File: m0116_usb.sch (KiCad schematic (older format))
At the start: 182 parts, among them J1 AVR-ISP-6, J2 Conn_01x04, J3 Conn_01x04, U1 ATmega32A-PU

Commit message: change ucontroller to ATmega32u4
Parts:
- removed Boot1: Boot, Button_Switch_THT:SW_PUSH_6mm, symbol Switch:SW_Push
- removed C1: 4.7u, Capacitor_THT:CP_Radial_D5.0mm_P2.50mm, symbol Device:CP1
- removed C2, C3: 0.1u, Capacitor_THT:C_Disc_D3.0mm_W2.0mm_P2.50mm, symbol Device:C
- removed U1: ATmega32A-PU, Package_DIP:DIP-40_W15.24mm_Socket, symbol MCU_Microchip_ATmega:ATmega32A-PU
- removed XTAL1: Crystal, Crystal:Crystal_HC49-4H_Vertical, symbol Device:Crystal
- added C?: 1u, symbol Device:C_Small
- added C? (x4): 0.1u, Capacitor_THT:C_Disc_D6.0mm_W2.5mm_P5.00mm, symbol Device:C_Small
- added C?: 10u, Capacitor_THT:C_Disc_D6.0mm_W2.5mm_P5.00mm, symbol Device:C_Small
- added R?: 10k, Resistor_THT:R_Axial_DIN0207_L6.3mm_D2.5mm_P10.16mm_Horizontal, symbol Device:R
- added U?: ATmega32U4-AU, Package_QFP:TQFP-44_10x10mm_P0.8mm, symbol MCU_Microchip_ATmega:ATmega32U4-AU
- added X?: Crystal, symbol Device:Crystal_GND24_Small
- D10, D11, D12, D13, D14, D15, D16, D17, D18, D19, D20, D21, D22, D23, D24, D25, D26, D27, D28, D29, D3, D30, D31, D32, D33, D34, D35, D36, D37, D38, D39, D4, D40, D41, D42, D43, D44, D45, D46, D47, D48, D49, D5, D50, D51, D52, D53, D54, D55, D56, D57, D58, D59, D6, D60, D61, D62, D63, D64, D65, D66, D67, D68, D69, D7, D70, D71, D72, D73, D74, D75, D76, D77, D78, D79, D8, D80, D81, D82, D83, D9: footprint Diode_THT:D_DO-35_SOD27_P7.62mm_Horizontal -> Diode_SMD:D_SOD-123
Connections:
- net labels added: XTAL1, XTAL2
- net labels removed: boot
- wire segments 280 -> 308
- no-connect marks 0 -> 4
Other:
- moved on the sheet: C4, C5, D1, D10, D11, D12, D13, D14, D15, D16, D17, D18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

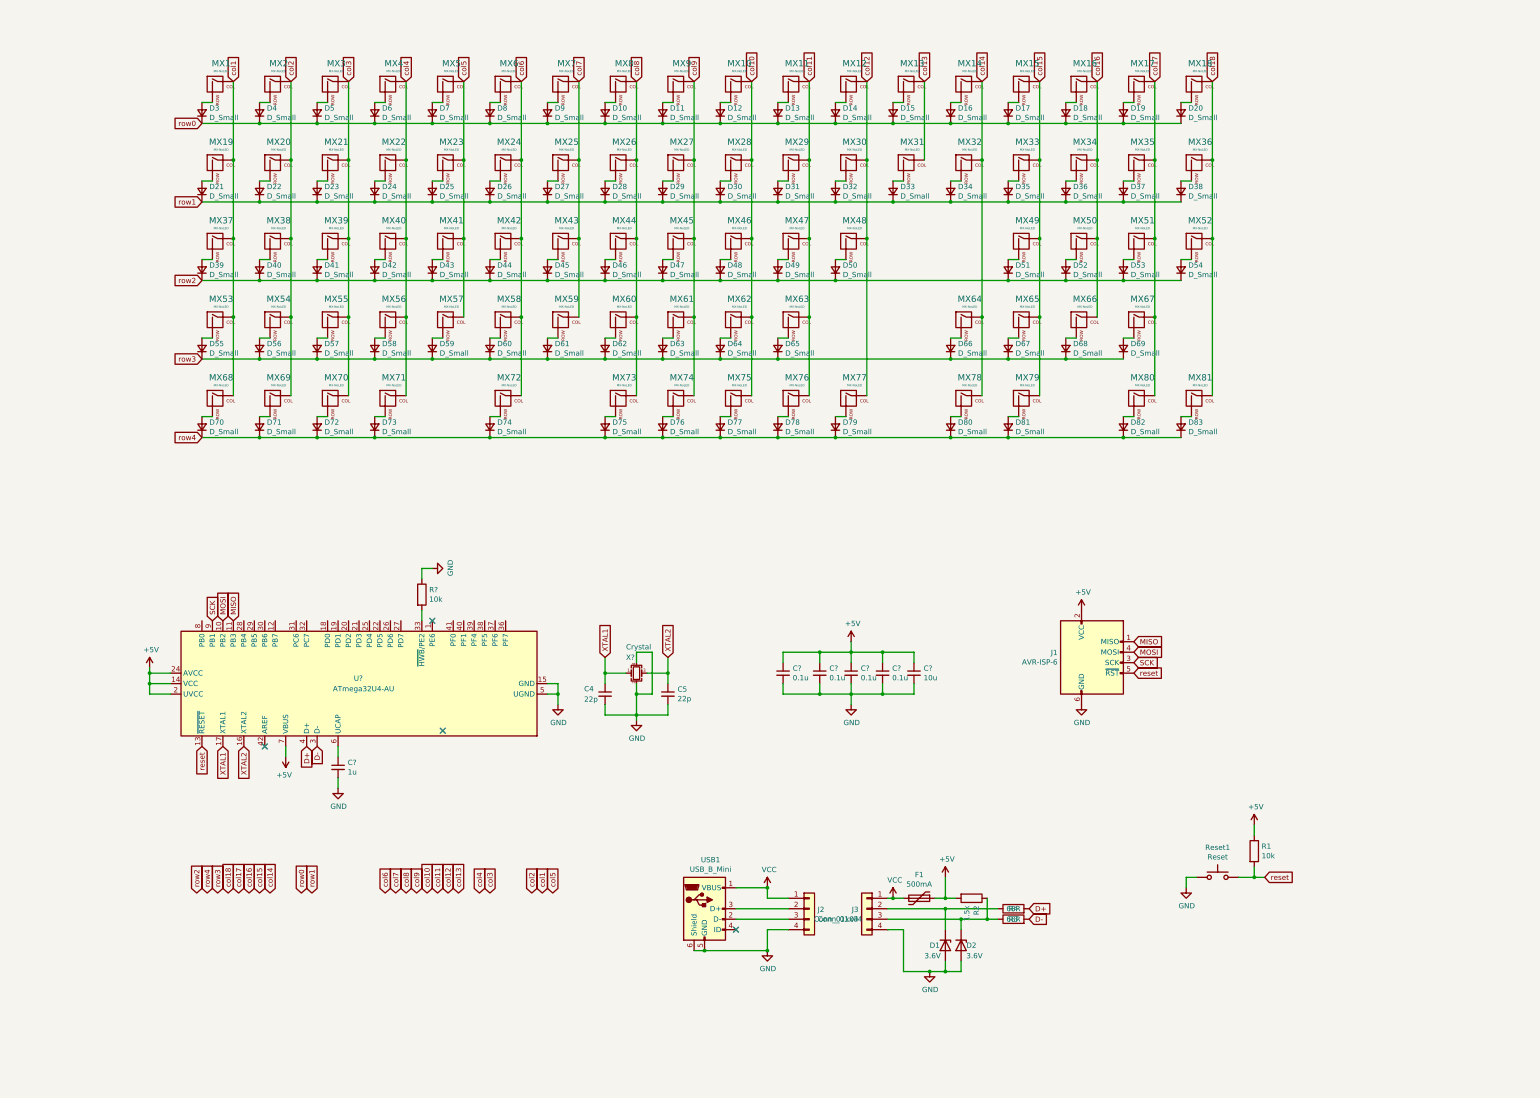
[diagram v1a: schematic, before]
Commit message: populate smd components, routing, finalize rev2
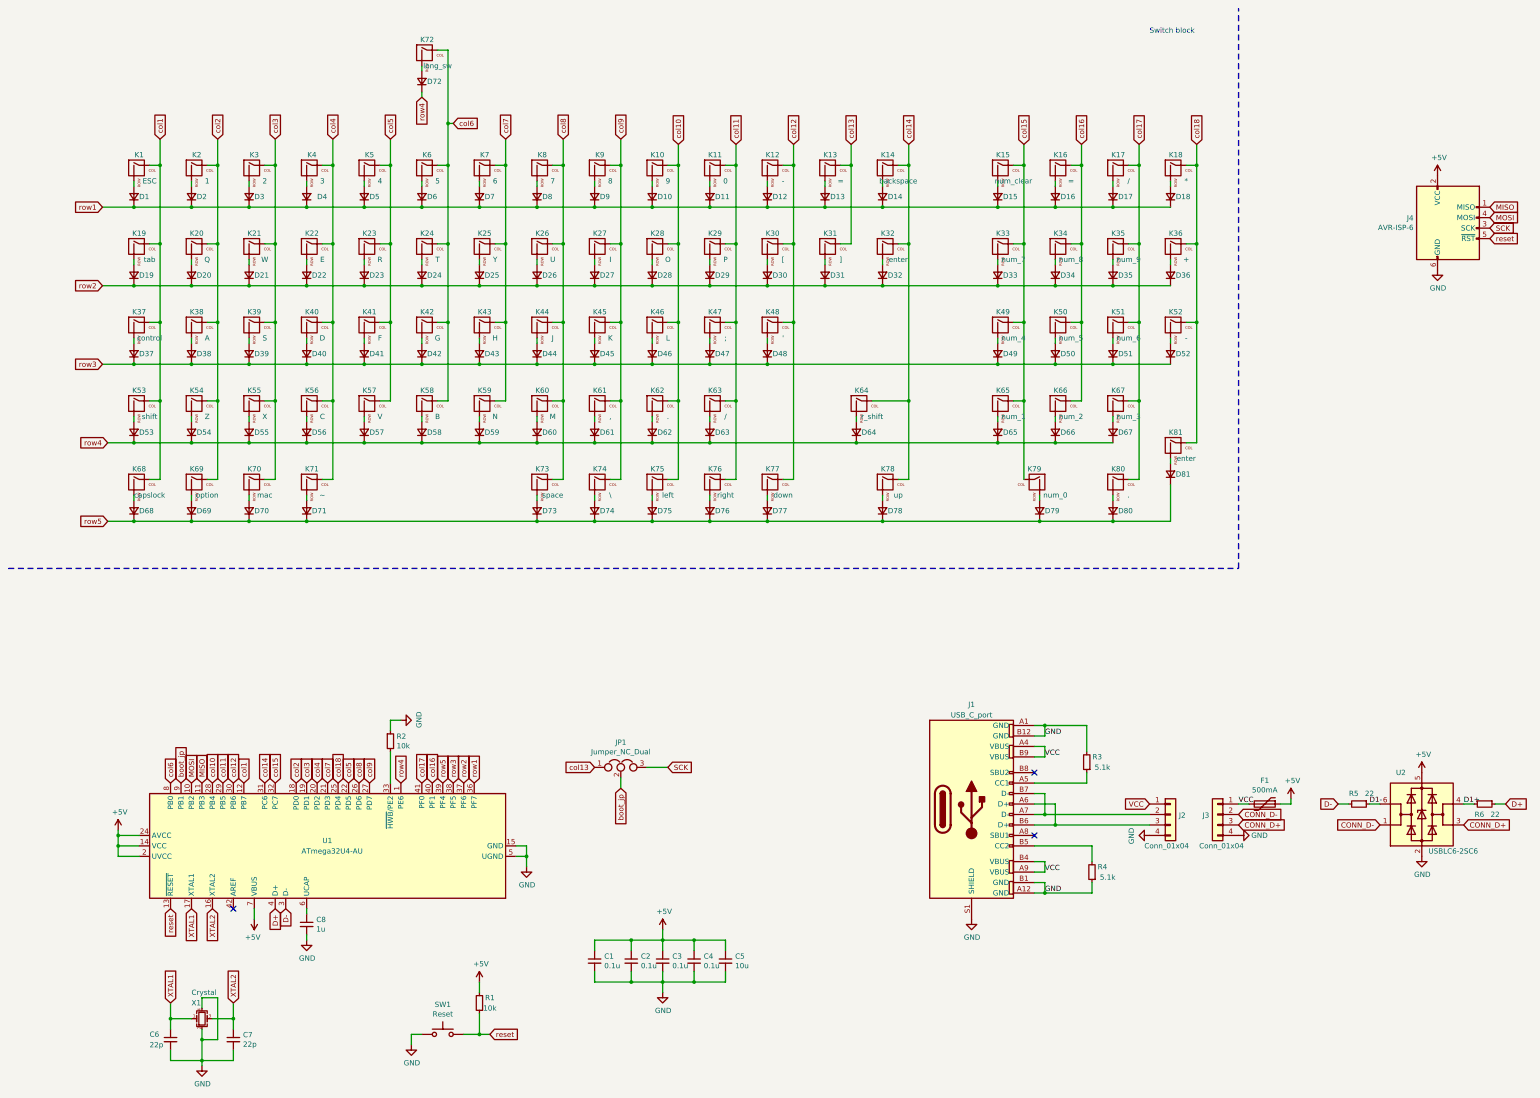
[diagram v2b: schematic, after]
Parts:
- removed D1, D2: 3.6V, Diode_THT:D_DO-35_SOD27_P7.62mm_Horizontal, symbol Device:D_Zener
- removed MX1, MX10, MX11, MX12, MX13, MX14, MX15, MX16, MX17, MX18, MX19, MX2, MX20, MX21, MX22, MX23, MX24, MX25, MX26, MX27, MX28, MX29, MX3, MX30, MX31, MX32, MX33, MX34, MX35, MX36, MX37, MX38, MX39, MX4, MX40, MX41, MX42, MX43, MX44, MX45, MX46, MX47, MX48, MX49, MX5, MX50, MX51, MX52, MX53, MX54, MX55, MX56, MX57, MX58, MX59, MX6, MX60, MX61, MX62, MX63, MX64, MX65, MX66, MX67, MX68, MX69, MX7, MX70, MX71, MX72, MX73, MX74, MX75, MX76, MX77, MX78, MX79, MX8, MX80, MX81, MX9: MX-NoLED, project_custom_parts:ALPS-1U, symbol m0116_usb-rescue:MX-NoLED
- removed R1, R?: 10k, Resistor_THT:R_Axial_DIN0207_L6.3mm_D2.5mm_P10.16mm_Horizontal, symbol Device:R
- removed R2: 1.5k, Resistor_THT:R_Axial_DIN0207_L6.3mm_D2.5mm_P10.16mm_Horizontal, symbol Device:R
- removed R3, R4: 68R, Resistor_THT:R_Axial_DIN0207_L6.3mm_D2.5mm_P10.16mm_Horizontal, symbol Device:R
- removed USB1: USB_B_Mini, project_custom_parts:Molex-0548190519, symbol Connector:USB_B_Mini
- added J1: USB_C_port, Connector_USB:USB_C_Receptacle_XKB_U262-16XN-4BVC11, symbol m0116_project:USB_C_port
- added JP1: Jumper_NC_Dual, Jumper:SolderJumper-3_P1.3mm_Bridged12_Pad1.0x1.5mm, symbol Device:Jumper_NC_Dual
- added K1: ESC, project_custom_parts:ALPS-1U, symbol m0116_project:MX-NoLED
- added K10: 9, project_custom_parts:ALPS-1U, symbol m0116_project:MX-NoLED
- added K11: 0, project_custom_parts:ALPS-1U, symbol m0116_project:MX-NoLED
- added K12, K52: -, project_custom_parts:ALPS-1U, symbol m0116_project:MX-NoLED
- added K13, K16: =, project_custom_parts:ALPS-1U, symbol m0116_project:MX-NoLED
- added K14: backspace, project_custom_parts:ALPS-1U, symbol m0116_project:MX-NoLED
- added K15: num_clear, project_custom_parts:ALPS-1U, symbol m0116_project:MX-NoLED
- added K17, K63: /, project_custom_parts:ALPS-1U, symbol m0116_project:MX-NoLED
- added K18: *, project_custom_parts:ALPS-1U, symbol m0116_project:MX-NoLED
- added K19: tab, project_custom_parts:ALPS-1U, symbol m0116_project:MX-NoLED
- added K2: 1, project_custom_parts:ALPS-1U, symbol m0116_project:MX-NoLED
- added K20: Q, project_custom_parts:ALPS-1U, symbol m0116_project:MX-NoLED
- added K21: W, project_custom_parts:ALPS-1U, symbol m0116_project:MX-NoLED
- added K22: E, project_custom_parts:ALPS-1U, symbol m0116_project:MX-NoLED
- added K23: R, project_custom_parts:ALPS-1U, symbol m0116_project:MX-NoLED
- added K24: T, project_custom_parts:ALPS-1U, symbol m0116_project:MX-NoLED
- added K25: Y, project_custom_parts:ALPS-1U, symbol m0116_project:MX-NoLED
- added K26: U, project_custom_parts:ALPS-1U, symbol m0116_project:MX-NoLED
- added K27: I, project_custom_parts:ALPS-1U, symbol m0116_project:MX-NoLED
- added K28: O, project_custom_parts:ALPS-1U, symbol m0116_project:MX-NoLED
- added K29: P, project_custom_parts:ALPS-1U, symbol m0116_project:MX-NoLED
- added K3: 2, project_custom_parts:ALPS-1U, symbol m0116_project:MX-NoLED
- added K30: [, project_custom_parts:ALPS-1U, symbol m0116_project:MX-NoLED
- added K31: ], project_custom_parts:ALPS-1U, symbol m0116_project:MX-NoLED
- added K32, K81: enter, project_custom_parts:ALPS-1U, symbol m0116_project:MX-NoLED
- added K33: num_7, project_custom_parts:ALPS-1U, symbol m0116_project:MX-NoLED
- added K34: num_8, project_custom_parts:ALPS-1U, symbol m0116_project:MX-NoLED
- added K35: num_9, project_custom_parts:ALPS-1U, symbol m0116_project:MX-NoLED
- added K36: +, project_custom_parts:ALPS-1U, symbol m0116_project:MX-NoLED
- added K37: control, project_custom_parts:ALPS-1U, symbol m0116_project:MX-NoLED
- added K38: A, project_custom_parts:ALPS-1U, symbol m0116_project:MX-NoLED
- added K39: S, project_custom_parts:ALPS-1U, symbol m0116_project:MX-NoLED
- added K4: 3, project_custom_parts:ALPS-1U, symbol m0116_project:MX-NoLED
- added K40: D, project_custom_parts:ALPS-1U, symbol m0116_project:MX-NoLED
- added K41: F, project_custom_parts:ALPS-1U, symbol m0116_project:MX-NoLED
- added K42: G, project_custom_parts:ALPS-1U, symbol m0116_project:MX-NoLED
- added K43: H, project_custom_parts:ALPS-1U, symbol m0116_project:MX-NoLED
- added K44: J, project_custom_parts:ALPS-1U, symbol m0116_project:MX-NoLED
- added K45: K, project_custom_parts:ALPS-1U, symbol m0116_project:MX-NoLED
- added K46: L, project_custom_parts:ALPS-1U, symbol m0116_project:MX-NoLED
- added K47: ;, project_custom_parts:ALPS-1U, symbol m0116_project:MX-NoLED
- added K48: ', project_custom_parts:ALPS-1U, symbol m0116_project:MX-NoLED
- added K49: num_4, project_custom_parts:ALPS-1U, symbol m0116_project:MX-NoLED
- added K5: 4, project_custom_parts:ALPS-1U, symbol m0116_project:MX-NoLED
- added K50: num_5, project_custom_parts:ALPS-1U, symbol m0116_project:MX-NoLED
- added K51: num_6, project_custom_parts:ALPS-1U, symbol m0116_project:MX-NoLED
- added K53: shift, project_custom_parts:ALPS-1U, symbol m0116_project:MX-NoLED
- added K54: Z, project_custom_parts:ALPS-1U, symbol m0116_project:MX-NoLED
- added K55: X, project_custom_parts:ALPS-1U, symbol m0116_project:MX-NoLED
- added K56: C, project_custom_parts:ALPS-1U, symbol m0116_project:MX-NoLED
- added K57: V, project_custom_parts:ALPS-1U, symbol m0116_project:MX-NoLED
- added K58: B, project_custom_parts:ALPS-1U, symbol m0116_project:MX-NoLED
- added K59: N, project_custom_parts:ALPS-1U, symbol m0116_project:MX-NoLED
- added K6: 5, project_custom_parts:ALPS-1U, symbol m0116_project:MX-NoLED
- added K60: M, project_custom_parts:ALPS-1U, symbol m0116_project:MX-NoLED
- added K61: ,, project_custom_parts:ALPS-1U, symbol m0116_project:MX-NoLED
- added K62, K80: ., project_custom_parts:ALPS-1U, symbol m0116_project:MX-NoLED
- added K64: r_shift, project_custom_parts:ALPS-1U, symbol m0116_project:MX-NoLED
- added K65: num_1, project_custom_parts:ALPS-1U, symbol m0116_project:MX-NoLED
- added K66: num_2, project_custom_parts:ALPS-1U, symbol m0116_project:MX-NoLED
- added K67: num_3, project_custom_parts:ALPS-1U, symbol m0116_project:MX-NoLED
- added K68: capslock, project_custom_parts:ALPS-1U, symbol m0116_project:MX-NoLED
- added K69: option, project_custom_parts:ALPS-1U, symbol m0116_project:MX-NoLED
- added K7: 6, project_custom_parts:ALPS-1U, symbol m0116_project:MX-NoLED
- added K70: mac, project_custom_parts:ALPS-1U, symbol m0116_project:MX-NoLED
- added K71: ~~, project_custom_parts:ALPS-1U, symbol m0116_project:MX-NoLED
- added K72: long_sw, project_custom_parts:ALPS-1U, symbol m0116_project:MX-NoLED
- added K73: space, project_custom_parts:ALPS-1U, symbol m0116_project:MX-NoLED
- added K74: \\, project_custom_parts:ALPS-1U, symbol m0116_project:MX-NoLED
- added K75: left, project_custom_parts:ALPS-1U, symbol m0116_project:MX-NoLED
- added K76: right, project_custom_parts:ALPS-1U, symbol m0116_project:MX-NoLED
- added K77: down, project_custom_parts:ALPS-1U, symbol m0116_project:MX-NoLED
- added K78: up, project_custom_parts:ALPS-1U, symbol m0116_project:MX-NoLED
- added K79: num_0, project_custom_parts:ALPS-1U, symbol m0116_project:MX-NoLED
- added K8: 7, project_custom_parts:ALPS-1U, symbol m0116_project:MX-NoLED
- added K9: 8, project_custom_parts:ALPS-1U, symbol m0116_project:MX-NoLED
- added R1, R2: 10k, Resistor_SMD:R_0603_1608Metric, symbol Device:R_Small
- added R3, R4: 5.1k, Resistor_SMD:R_0402_1005Metric, symbol Device:R_Small
- added R5, R6: 22, Resistor_SMD:R_0603_1608Metric, symbol Device:R_Small
- added U2: USBLC6-2SC6, Package_TO_SOT_SMD:SOT-23-6, symbol Power_Protection:USBLC6-2SC6
- C1, C2, C3, C4, C5: renamed from C?; footprint Capacitor_THT:C_Disc_D6.0mm_W2.5mm_P5.00mm -> Capacitor_SMD:C_0603_1608Metric
- C6: renamed from C4; footprint Capacitor_THT:C_Disc_D6.0mm_W2.5mm_P5.00mm -> Capacitor_SMD:C_0402_1005Metric
- C7: renamed from C5; footprint Capacitor_THT:C_Disc_D6.0mm_W2.5mm_P5.00mm -> Capacitor_SMD:C_0402_1005Metric
- C8: renamed from C?; footprint (none) -> Capacitor_SMD:C_0402_1005Metric
- F1: footprint Fuse:Fuse_Littelfuse_395Series -> Fuse:Fuse_1206_3216Metric_Castellated
- J2: footprint Connector_PinHeader_2.00mm:PinHeader_1x04_P2.00mm_Vertical -> Connector_PinHeader_1.00mm:PinHeader_1x04_P1.00mm_Vertical
- J3: footprint Connector_JST:JST_PH_S4B-PH-K_1x04_P2.00mm_Horizontal -> project_custom_parts:PinSocket_1x04_P1.00mm_Vertical_SMD
- J4: renamed from J1; footprint Connector_PinHeader_2.54mm:PinHeader_2x03_P2.54mm_Horizontal -> Connector_IDC:IDC-Header_2x03_P2.54mm_Vertical
- SW1: renamed from Reset1; footprint Button_Switch_THT:SW_PUSH_6mm -> Button_Switch_SMD:SW_SPST_TL3342
- X1: renamed from X?; footprint (none) -> Crystal:Crystal_SMD_3225-4Pin_3.2x2.5mm
- gave numbers to parts that had none: 1
- renumbered D3 to D1, D12 to D10, D13 to D11, D14 to D12, D15 to D13, D16 to D14, D17 to D15, D18 to D16, D19 to D17, D20 to D18, D21 to D19, D4 to D2, D22 to D20, D23 to D21, D24 to D22, D25 to D23, D26 to D24, D27 to D25, D28 to D26, D29 to D27, D30 to D28, D31 to D29, D5 to D3, D32 to D30, D33 to D31, D34 to D32, D35 to D33, D36 to D34, D37 to D35, D38 to D36, D39 to D37, D40 to D38, D41 to D39, D6 to D4, D42 to D40, D43 to D41, D44 to D42, D45 to D43, D46 to D44, D47 to D45, D48 to D46, D49 to D47, D50 to D48, D51 to D49, D7 to D5, D52 to D50, D53 to D51, D54 to D52, D55 to D53, D56 to D54, D57 to D55, D58 to D56, D59 to D57, D60 to D58, D61 to D59, D8 to D6, D62 to D60, D63 to D61, D64 to D62, D65 to D63, D66 to D64, D67 to D65, D68 to D66, D69 to D67, D70 to D68, D71 to D69, D9 to D7, D72 to D70, D73 to D71, D74 to D72, D75 to D73, D76 to D74, D77 to D75, D78 to D76, D79 to D77, D80 to D78, D81 to D79, D10 to D8, D82 to D80, D83 to D81, D11 to D9
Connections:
- net row0 is gone; now on net row1: D1.1 (K), D10.1 (K), D11.1 (K), D12.1 (K), D13.1 (K), D14.1 (K), D15.1 (K), D16.1 (K), D17.1 (K), D18.1 (K), D2.1 (K), D3.1 (K), D4.1 (K), D5.1 (K), D6.1 (K), D7.1 (K), D8.1 (K), D9.1 (K)
- net +5V: now also R1.2, U2.5 (VBUS)
- net D+: now also R6.1
- net D-: now also R5.2
- net GND: now also J1.A1 (GND), J1.A12 (GND), J1.B1 (GND), J1.B12 (GND), J1.S1 (SHIELD), R2.1, R3.2, R4.1, U2.2 (GND)
- net SCK: now also JP1.3; no longer U1.9 (PB1)
- net VCC: now also J1.A4 (VBUS), J1.A9 (VBUS), J1.B4 (VBUS), J1.B9 (VBUS)
- net col1: now also U1.12 (PB7), K1.1 (COL), K19.1 (COL), K37.1 (COL), K53.1 (COL), K68.1 (COL)
- net col10: now also U1.28 (PB4), K10.1 (COL), K28.1 (COL), K46.1 (COL), K62.1 (COL), K75.1 (COL)
- net col11: now also U1.29 (PB5), K11.1 (COL), K29.1 (COL), K47.1 (COL), K63.1 (COL), K76.1 (COL)
- net col12: now also U1.30 (PB6), K12.1 (COL), K30.1 (COL), K48.1 (COL), K77.1 (COL)
- net col13: now also JP1.1, K13.1 (COL), K31.1 (COL)
- net col14: now also U1.31 (PC6), K14.1 (COL), K32.1 (COL), K64.1 (COL), K78.1 (COL)
- net col15: now also U1.32 (PC7), K15.1 (COL), K33.1 (COL), K49.1 (COL), K65.1 (COL), K79.1 (COL)
- net col16: now also U1.40 (PF1), K16.1 (COL), K34.1 (COL), K50.1 (COL), K66.1 (COL)
- net col17: now also U1.41 (PF0), K17.1 (COL), K35.1 (COL), K51.1 (COL), K67.1 (COL), K80.1 (COL)
- net col18: now also U1.25 (PD4), K18.1 (COL), K36.1 (COL), K52.1 (COL), K81.1 (COL)
- net col2: now also U1.18 (PD0), K2.1 (COL), K20.1 (COL), K38.1 (COL), K54.1 (COL), K69.1 (COL)
- net col3: now also U1.19 (PD1), K21.1 (COL), K3.1 (COL), K39.1 (COL), K55.1 (COL), K70.1 (COL)
- net col4: now also U1.20 (PD2), K22.1 (COL), K4.1 (COL), K40.1 (COL), K56.1 (COL), K71.1 (COL)
- net col5: now also U1.22 (PD5), K23.1 (COL), K41.1 (COL), K5.1 (COL), K57.1 (COL)
- net col6: now also U1.8 (PB0), K24.1 (COL), K42.1 (COL), K58.1 (COL), K6.1 (COL), K72.1 (COL)
- net col7: now also U1.21 (PD3), K25.1 (COL), K43.1 (COL), K59.1 (COL), K7.1 (COL)
- net col8: now also U1.26 (PD6), K26.1 (COL), K44.1 (COL), K60.1 (COL), K73.1 (COL), K8.1 (COL)
- net col9: now also U1.27 (PD7), K27.1 (COL), K45.1 (COL), K61.1 (COL), K74.1 (COL), K9.1 (COL)
- net reset: now also R1.1
- net row1: now also U1.36 (PF7); no longer D19.1 (K), D20.1 (K), D21.1 (K), D22.1 (K), D23.1 (K), D24.1 (K), D25.1 (K), D26.1 (K), D27.1 (K), D28.1 (K), D29.1 (K), D30.1 (K), D31.1 (K), D32.1 (K), D33.1 (K), D34.1 (K), D35.1 (K), D36.1 (K)
- net row2: now also D19.1 (K), D20.1 (K), D21.1 (K), D22.1 (K), D23.1 (K), D24.1 (K), D25.1 (K), D26.1 (K), D27.1 (K), D28.1 (K), D29.1 (K), D30.1 (K), D31.1 (K), D32.1 (K), D33.1 (K), D34.1 (K), D35.1 (K), D36.1 (K), U1.37 (PF6); no longer D37.1 (K), D38.1 (K), D39.1 (K), D40.1 (K), D41.1 (K), D42.1 (K), D43.1 (K), D44.1 (K), D45.1 (K), D46.1 (K), D47.1 (K), D48.1 (K), D49.1 (K), D50.1 (K), D51.1 (K), D52.1 (K)
- net row3: now also D37.1 (K), D38.1 (K), D39.1 (K), D40.1 (K), D41.1 (K), D42.1 (K), D43.1 (K), D44.1 (K), D45.1 (K), D46.1 (K), D47.1 (K), D48.1 (K), D49.1 (K), D50.1 (K), D51.1 (K), D52.1 (K), U1.38 (PF5); no longer D53.1 (K), D54.1 (K), D55.1 (K), D56.1 (K), D57.1 (K), D58.1 (K), D59.1 (K), D60.1 (K), D61.1 (K), D62.1 (K), D63.1 (K), D64.1 (K), D65.1 (K), D66.1 (K), D67.1 (K)
- net row4: now also D53.1 (K), D54.1 (K), D55.1 (K), D56.1 (K), D57.1 (K), D58.1 (K), D59.1 (K), D60.1 (K), D61.1 (K), D62.1 (K), D63.1 (K), D64.1 (K), D65.1 (K), D66.1 (K), D67.1 (K), U1.1 (PE6); no longer D68.1 (K), D69.1 (K), D70.1 (K), D71.1 (K), D73.1 (K), D74.1 (K), D75.1 (K), D76.1 (K), D77.1 (K), D78.1 (K), D79.1 (K), D80.1 (K), D81.1 (K)
- net CONN_D-: now reaches J3.2 (Pin_2)
- net CONN_D-: now also U2.1 (I/O1)
- net CONN_D+: now reaches J3.3 (Pin_3)
- net CONN_D+: now also U2.3 (I/O2)
- net at J2.3 (Pin_3): now also J1.A6 (D+), J1.B6 (D+)
- net at J2.2 (Pin_2): now also J1.A7 (D-), J1.B7 (D-)
- net at D1.2 (A): now also K1.2 (ROW)
- net at D2.2 (A): now also K2.2 (ROW)
- net at D3.2 (A): now also K3.2 (ROW)
- net at D4.2 (A): now also K4.2 (ROW)
- net at D5.2 (A): now also K5.2 (ROW)
- net at D6.2 (A): now also K6.2 (ROW)
- net at D7.2 (A): now also K7.2 (ROW)
- net at D8.2 (A): now also K8.2 (ROW)
- net at D9.2 (A): now also K9.2 (ROW)
- net at D10.2 (A): now also K10.2 (ROW)
- net at D11.2 (A): now also K11.2 (ROW)
- net at D12.2 (A): now also K12.2 (ROW)
- net at D13.2 (A): now also K13.2 (ROW)
- net at D14.2 (A): now also K14.2 (ROW)
- net at D15.2 (A): now also K15.2 (ROW)
- net at D16.2 (A): now also K16.2 (ROW)
- net at D17.2 (A): now also K17.2 (ROW)
- net at D18.2 (A): now also K18.2 (ROW)
- net at D19.2 (A): now also K19.2 (ROW)
- net at D20.2 (A): now also K20.2 (ROW)
- net at D21.2 (A): now also K21.2 (ROW)
- net at D22.2 (A): now also K22.2 (ROW)
- net at D23.2 (A): now also K23.2 (ROW)
- net at D24.2 (A): now also K24.2 (ROW)
- net at D25.2 (A): now also K25.2 (ROW)
- net at D26.2 (A): now also K26.2 (ROW)
- net at D27.2 (A): now also K27.2 (ROW)
- net at D28.2 (A): now also K28.2 (ROW)
- net at D29.2 (A): now also K29.2 (ROW)
- net at D30.2 (A): now also K30.2 (ROW)
- net at D31.2 (A): now also K31.2 (ROW)
- net at D32.2 (A): now also K32.2 (ROW)
- net at D33.2 (A): now also K33.2 (ROW)
- net at D34.2 (A): now also K34.2 (ROW)
- net at D35.2 (A): now also K35.2 (ROW)
- net at D36.2 (A): now also K36.2 (ROW)
- net at D37.2 (A): now also K37.2 (ROW)
- net at D38.2 (A): now also K38.2 (ROW)
- net at D39.2 (A): now also K39.2 (ROW)
- net at D40.2 (A): now also K40.2 (ROW)
- net at D41.2 (A): now also K41.2 (ROW)
- net at D42.2 (A): now also K42.2 (ROW)
- net at D43.2 (A): now also K43.2 (ROW)
- net at D44.2 (A): now also K44.2 (ROW)
- net at D45.2 (A): now also K45.2 (ROW)
- net at D46.2 (A): now also K46.2 (ROW)
- net at D47.2 (A): now also K47.2 (ROW)
- net at D48.2 (A): now also K48.2 (ROW)
- net at D49.2 (A): now also K49.2 (ROW)
- net at D50.2 (A): now also K50.2 (ROW)
- net at D51.2 (A): now also K51.2 (ROW)
- net at D52.2 (A): now also K52.2 (ROW)
- net at D53.2 (A): now also K53.2 (ROW)
- net at D54.2 (A): now also K54.2 (ROW)
- net at D55.2 (A): now also K55.2 (ROW)
- net at D56.2 (A): now also K56.2 (ROW)
- net at D57.2 (A): now also K57.2 (ROW)
- net at D58.2 (A): now also K58.2 (ROW)
- net at D59.2 (A): now also K59.2 (ROW)
- net at D60.2 (A): now also K60.2 (ROW)
- net at D61.2 (A): now also K61.2 (ROW)
- net at D62.2 (A): now also K62.2 (ROW)
- net at D63.2 (A): now also K63.2 (ROW)
- net at D64.2 (A): now also K64.2 (ROW)
- net at D65.2 (A): now also K65.2 (ROW)
- net at D66.2 (A): now also K66.2 (ROW)
- net at D67.2 (A): now also K67.2 (ROW)
- net at D68.2 (A): now also K68.2 (ROW)
- net at D69.2 (A): now also K69.2 (ROW)
- net at D70.2 (A): now also K70.2 (ROW)
- net at D71.2 (A): now also K71.2 (ROW)
- net at D73.2 (A): now also K73.2 (ROW)
- net at D74.2 (A): now also K74.2 (ROW)
- net at D75.2 (A): now also K75.2 (ROW)
- net at D76.2 (A): now also K76.2 (ROW)
- net at D77.2 (A): now also K77.2 (ROW)
- net at D78.2 (A): now also K78.2 (ROW)
- net at D79.2 (A): now also K79.2 (ROW)
- net at D80.2 (A): now also K80.2 (ROW)
- net at D81.2 (A): now also K81.2 (ROW)
- net at D72.2 (A): now also K72.2 (ROW)
- net at U1.33 (~HWB~/PE2): now also R2.2
- net row5: now reaches U1.39 (PF4)
- net row5: now also D68.1 (K), D69.1 (K), D70.1 (K), D71.1 (K), D73.1 (K), D74.1 (K), D75.1 (K), D76.1 (K), D77.1 (K), D78.1 (K), D79.1 (K), D80.1 (K), D81.1 (K)
- new net: J1.A5 (CC1), R3.1
- new net: J1.B5 (CC2), R4.2
- new net D1+: R6.2, U2.4 (I/O2)
- new net D1-: R5.1, U2.6 (I/O1)
- new net boot_jp: JP1.2, U1.9 (PB1)
- no-connect marks 4 -> 3
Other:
- note added: "Switch block"
- moved on the sheet: C1, C2, C3, C4, C5, C6, C7, C8, D1, D10, D11, D12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

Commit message: replace smd jumper with spdt switch
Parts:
- removed JP1: Jumper_NC_Dual, Jumper:SolderJumper-3_P1.3mm_Bridged12_Pad1.0x1.5mm, symbol Device:Jumper_NC_Dual
- added SW2: SW_SPDT, Button_Switch_SMD:SW_SPDT_CK-JS102011SAQN, symbol Switch:SW_SPDT
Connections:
- net SCK: now also SW2.3 (C)
- net boot_jp: now also SW2.2 (B)
- net col13: now also SW2.1 (A)
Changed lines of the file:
@@
 Text GLabel 2200 7850 1    50   Input ~ 0
 MOSI
-Wire Wire Line
-	6750 7700 6550 7700
-Text GLabel 6750 7700 2    50   Input ~ 0
+Text GLabel 14350 3850 2    50   Input ~ 0
 SCK
 Text GLabel 2100 7850 1    50   Input ~ 0
 boot_jp
-Text GLabel 6300 7900 3    50   Input ~ 0
+Text GLabel 13950 3750 0    50   Input ~ 0
 boot_jp
-Wire Wire Line
-	6300 7900 6300 7800
 Wire Wire Line
 	3300 5350 5500 5350
@@
 Wire Wire Line
 	4550 850  4650 850
-$Comp
-L Device:Jumper_NC_Dual JP1
-U 1 1 62328914
-P 6300 7700
-F 0 "JP1" H 6300 7939 50  0000 C CNN
-F 1 "Jumper_NC_Dual" H 6300 7848 50  0000 C CNN
-F 2 "Jumper:SolderJumper-3_P1.3mm_Bridged12_Pad1.0x1.5mm" H 6300 7700 50  0001 C CNN
-F 3 "~" H 6300 7700 50  0001 C CNN
-	1    6300 7700
-	1    0    0    -1
-$EndComp
 $Comp
 L power:GND #PWR0101
@@
 Text GLabel 3700 7850 1    50   Input ~ 0
 col5
-Text GLabel 6050 7700 0    50   Input ~ 0
+Text GLabel 14350 3650 2    50   Input ~ 0
 col13
 Text GLabel 3300 7850 1    50   Input ~ 0
@@
 Text Label 13450 8050 0    50   ~ 0
 D1-
+$Comp
+L Switch:SW_SPDT SW2
+U 1 1 61528A13
+P 14150 3750
+F 0 "SW2" H 14150 4035 50  0000 C CNN
+F 1 "SW_SPDT" H 14150 3944 50  0000 C CNN
+F 2 "Button_Switch_SMD:SW_SPDT_CK-JS102011SAQN" H 14150 3750 50  0001 C CNN
+F 3 "~" H 14150 3750 50  0001 C CNN
+	1    14150 3750
+	1    0    0    -1
+$EndComp
 $EndSCHEMATC

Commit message: revise daughterboard, finalize
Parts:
- C1, C2, C3, C4: LCSC Part # (none) -> C14663; LCSC Part Number (none) -> C14663
- C5: LCSC Part # (none) -> C19702; LCSC Part Number (none) -> C19702
- C6, C7: LCSC Part # (none) -> C1555; LCSC Part Number (none) -> C1555
- C8: LCSC Part # (none) -> C52923; LCSC Part Number (none) -> C52923
- D1, D10, D11, D12, D13, D14, D15, D16, D17, D18, D19, D2, D20, D21, D22, D23, D24, D25, D26, D27, D28, D29, D3, D30, D31, D32, D33, D34, D35, D36, D37, D38, D39, D4, D40, D41, D42, D43, D44, D45, D46, D47, D48, D49, D5, D50, D51, D52, D53, D54, D55, D56, D57, D58, D59, D6, D60, D61, D62, D63, D64, D65, D66, D67, D68, D69, D7, D70, D71, D72, D73, D74, D75, D76, D77, D78, D79, D8, D80, D81, D9: LCSC Part # (none) -> C81598; LCSC Part Number (none) -> C81598
- F1: LCSC Part # (none) -> C135336; LCSC Part Number (none) -> C135336
- J1: LCSC Part # (none) -> C393939; LCSC Part Number (none) -> C393939
- J3: LCSC Part # (none) -> C239522; LCSC Part Number (none) -> C239522
- R1, R2: LCSC Part # (none) -> C25197; LCSC Part Number (none) -> C25197
- R3, R4: LCSC Part # (none) -> C23186; LCSC Part Number (none) -> C23186
- R5, R6: LCSC Part # (none) -> C23345; LCSC Part Number (none) -> C23345
- SW1: LCSC Part # (none) -> C318884; LCSC Part Number (none) -> C318884
- SW2: footprint Button_Switch_SMD:SW_SPDT_CK-JS102011SAQN -> project_custom_parts:SW_SPDT_SK-3245S-L1-A; LCSC Part # (none) -> C405951; LCSC Part Number (none) -> C405951
- U1: LCSC Part # (none) -> C44854; LCSC Part Number (none) -> C44854
- U2: LCSC Part # (none) -> C2687116; LCSC Part Number (none) -> C2687116
- X1: LCSC Part # (none) -> C160456; LCSC Part Number (none) -> C160456
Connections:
- net +5V: now also J2.1 (Pin_1), J3.1 (Pin_1)
- net CONN_D+: now also J2.3 (Pin_3), U2.4 (I/O2); no longer J3.3 (Pin_3), U2.3 (I/O2)
- net CONN_D-: now also J2.2 (Pin_2), U2.6 (I/O1); no longer J3.2 (Pin_2), U2.1 (I/O1)
- net D+: now also J3.3 (Pin_3); no longer U1.4 (D+)
- net D-: now also J3.2 (Pin_2), R5.1; no longer R5.2, U1.3 (D-)
- net VCC: no longer J2.1 (Pin_1), J3.1 (Pin_1)
- net at J1.A7 (D-), J1.B7 (D-): now also U2.1 (I/O1); no longer J2.2 (Pin_2)
- net USB_D+: now reaches J1.A6 (D+), J1.B6 (D+)
- net USB_D+: now also U2.3 (I/O2); no longer J2.3 (Pin_3)
- net D1+: no longer names the net of R6.2
- net D1+: now also U1.4 (D+); no longer U2.4 (I/O2)
- removed net D1-: R5.1, U2.6 (I/O1)
- new net: R5.2, U1.3 (D-)
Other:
- moved on the sheet: F1, J2, J3, R5, R6, U2
